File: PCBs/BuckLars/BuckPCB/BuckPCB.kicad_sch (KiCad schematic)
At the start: 91 parts, among them Q1 IRLIZ44N, Q2 IRLIZ44N, Q3 IRLIZ44N, Q4 IRLIZ44N, U1 ESP32-WROOM-32D, U2 LT1936, U3 LF2304NTR, U4 LF2304NTR, U5 LT1936

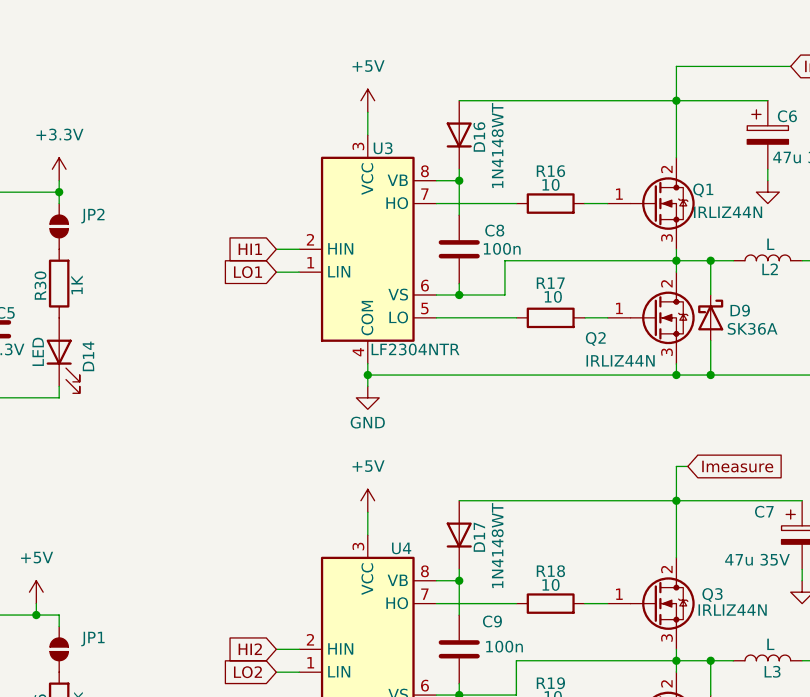
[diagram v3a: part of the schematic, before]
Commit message: changed supply of gate driver
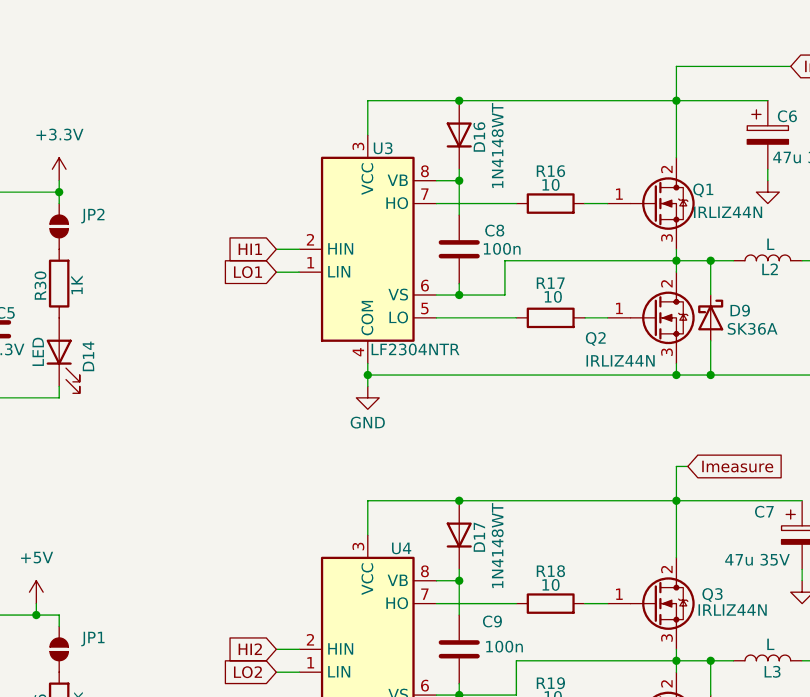
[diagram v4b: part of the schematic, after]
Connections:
- net +5V: no longer U3.3 (VCC), U4.3 (VCC)
- net Imeasure: now also U3.3 (VCC), U4.3 (VCC)
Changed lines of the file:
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@@
 	)
 	(junction
+		(at 173.99 21.59)
+		(diameter 0)
+		(color 0 0 0 0)
+	)
+	(junction
 		(at 29.21 36.83)
 		(diameter 0)
@@
 	)
 	(junction
+		(at 173.99 66.04)
+		(diameter 0)
+		(color 0 0 0 0)
+	)
+	(junction
 		(at 90.17 101.6)
 		(diameter 0)
@@
 	(wire
 		(pts
+			(xy 163.83 21.59) (xy 173.99 21.59)
+		)
+		(stroke
+			(width 0)
+			(type default)
+		)
+	)
+	(wire
+		(pts
 			(xy 171.45 33.02) (xy 180.34 33.02)
 		)
@@
 	(wire
 		(pts
-			(xy 163.83 22.86) (xy 163.83 25.4)
+			(xy 163.83 21.59) (xy 163.83 25.4)
 		)
 		(stroke
@@
 	(wire
 		(pts
-			(xy 163.83 67.31) (xy 163.83 69.85)
+			(xy 163.83 66.04) (xy 163.83 69.85)
 		)
 		(stroke
@@
 	(wire
 		(pts
+			(xy 163.83 66.04) (xy 173.99 66.04)
+		)
+		(stroke
+			(width 0)
+			(type default)
+		)
+	)
+	(wire
+		(pts
 			(xy 153.67 85.09) (xy 156.21 85.09)
 		)
@@
 	(symbol
 		(lib_id "power:+5V")
-		(at 163.83 67.31 0)
-		(unit 1)
-		(exclude_from_sim no)
-		(in_bom yes)
-		(on_board yes)
-		(dnp no)
-		(fields_autoplaced yes)
-		(property "Reference" "#PWR020"
-			(at 163.83 71.12 0)
-			(effects
-				(font
-					(size 1.27 1.27)
-				)
-				(hide yes)
-			)
-		)
-		(property "Value" "+5V"
-			(at 163.83 62.23 0)
-			(effects
-				(font
-					(size 1.27 1.27)
-				)
-			)
-		)
-		(property "Footprint" ""
-			(at 163.83 67.31 0)
-			(effects
-				(font
-					(size 1.27 1.27)
-				)
-				(hide yes)
-			)
-		)
-		(property "Datasheet" ""
-			(at 163.83 67.31 0)
-			(effects
-				(font
-					(size 1.27 1.27)
-				)
-				(hide yes)
-			)
-		)
-		(property "Description" "Power symbol creates a global label with name \"+5V\""
-			(at 163.83 67.31 0)
-			(effects
-				(font
-					(size 1.27 1.27)
-				)
-				(hide yes)
-			)
-		)
-		(pin "1"
-		)
-		(instances
-			(project "BuckPCB"
-				(path "/091e8063-b3c9-455e-bf2d-57e0600ed10e"
-					(reference "#PWR020")
-					(unit 1)
-				)
-			)
-		)
-	)
-	(symbol
-		(lib_id "power:+5V")
 		(at 242.57 134.62 90)
 		(unit 1)
@@
 					(unit 1)
 				)
-			)
-		)
-	)
-	(symbol
-		(lib_id "power:+5V")
-		(at 163.83 22.86 0)
-		(unit 1)
-		(exclude_from_sim no)
-		(in_bom yes)
-		(on_board yes)
-		(dnp no)
-		(fields_autoplaced yes)
-		(property "Reference" "#PWR022"
-			(at 163.83 26.67 0)
-			(effects
-				(font
-					(size 1.27 1.27)
-				)
-				(hide yes)
-			)
-		)
-		(property "Value" "+5V"
-			(at 163.83 17.78 0)
-			(effects
-				(font
-					(size 1.27 1.27)
-				)
-			)
-		)
-		(property "Footprint" ""
-			(at 163.83 22.86 0)
-			(effects
-				(font
-					(size 1.27 1.27)
-				)
-				(hide yes)
-			)
-		)
-		(property "Datasheet" ""
-			(at 163.83 22.86 0)
-			(effects
-				(font
-					(size 1.27 1.27)
-				)
-				(hide yes)
-			)
-		)
-		(property "Description" "Power symbol creates a global label with name \"+5V\""
-			(at 163.83 22.86 0)
-			(effects
-				(font
-					(size 1.27 1.27)
-				)
-				(hide yes)
-			)
-		)
-		(pin "1"
-		)
-		(instances
-			(project "BuckPCB"
-				(path "/091e8063-b3c9-455e-bf2d-57e0600ed10e"
-					(reference "#PWR022")
-					(unit 1)
-				)
